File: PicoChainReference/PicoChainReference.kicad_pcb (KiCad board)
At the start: 2 copper layers, 60 x 34 mm, 16 parts, among them J1 RJ45, J2 RJ45, J3 +12V, J4 +5V(M), J5 SCL, J6 +5V, U2 PCA9615DP, U3 LM78M05, U4 LM78M05, U5 LM1085-12

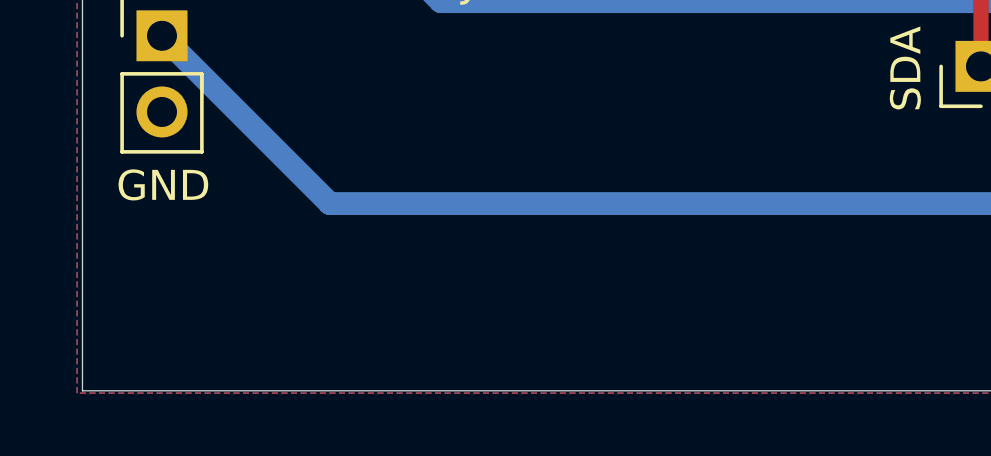
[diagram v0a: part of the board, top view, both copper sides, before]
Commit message: Finished off more reference designs and added readme
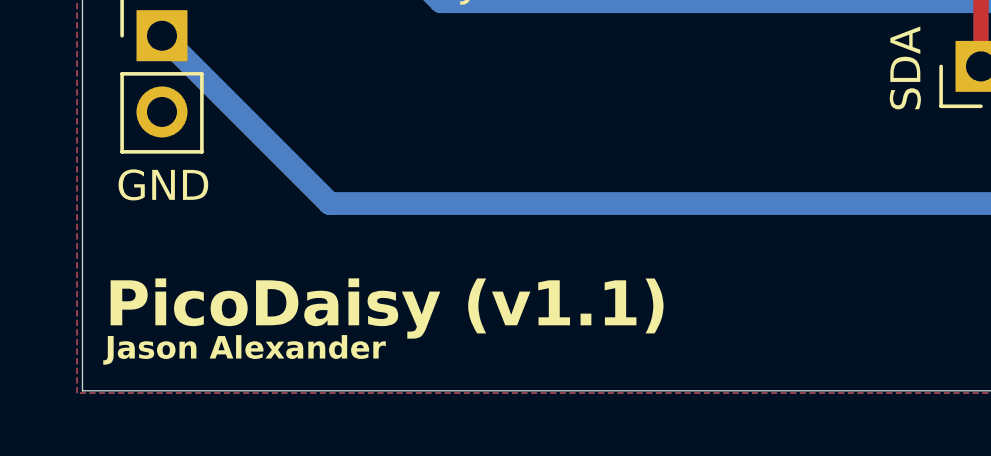
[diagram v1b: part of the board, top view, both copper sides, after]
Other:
- board text added: "Jason Alexander"
- board text added: "PicoDaisy (v1.1)"

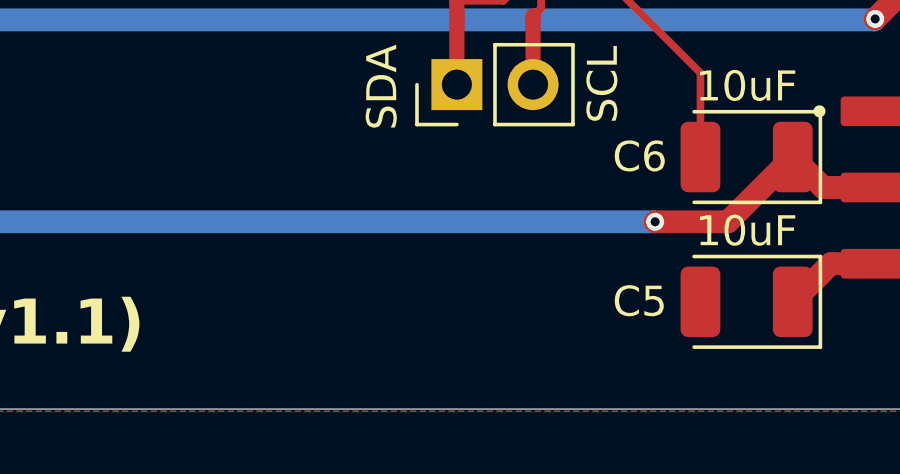
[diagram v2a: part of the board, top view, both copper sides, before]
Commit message: Added open source hardware logo to PCBs
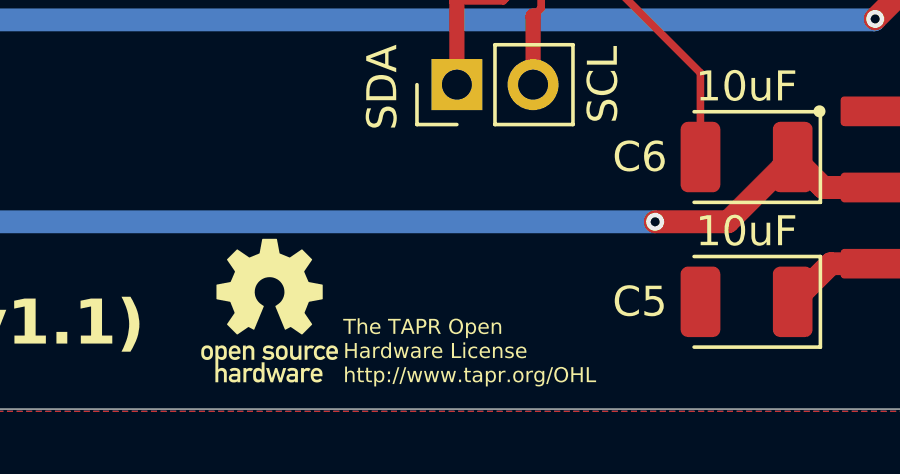
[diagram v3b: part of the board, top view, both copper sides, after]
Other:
- board text added: "The TAPR Open Hardware License http://www.tapr.org/OHL"

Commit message: Made pass through power rails larger.
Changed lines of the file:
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@@
 		(start 143.89475 86.99575)
 		(end 146.9545 83.936)
-		(width 0.762)
+		(width 1.016)
 		(layer "F.Cu")
 		(net 4)
@@
 		(start 143.8635 87.027)
 		(end 111.9455 87.027)
-		(width 0.762)
+		(width 1.016)
 		(layer "B.Cu")
 		(net 4)
@@
 		(start 111.9455 87.027)
 		(end 108.8545 83.936)
-		(width 0.762)
+		(width 1.016)
 		(layer "B.Cu")
 		(net 4)
@@
 		(start 116.4745 83.856)
 		(end 118.3755 85.757)
-		(width 0.762)
+		(width 1.016)
 		(layer "B.Cu")
 		(net 12)
@@
 		(start 118.3755 85.757)
 		(end 152.6735 85.757)
-		(width 0.762)
+		(width 1.016)
 		(layer "B.Cu")
 		(net 12)
@@
 		(start 152.6735 85.757)
 		(end 154.5745 83.856)
-		(width 0.762)
-		(layer "B.Cu")
-		(net 12)
+		(width 1.016)
+		(layer "B.Cu")
+		(net 12)

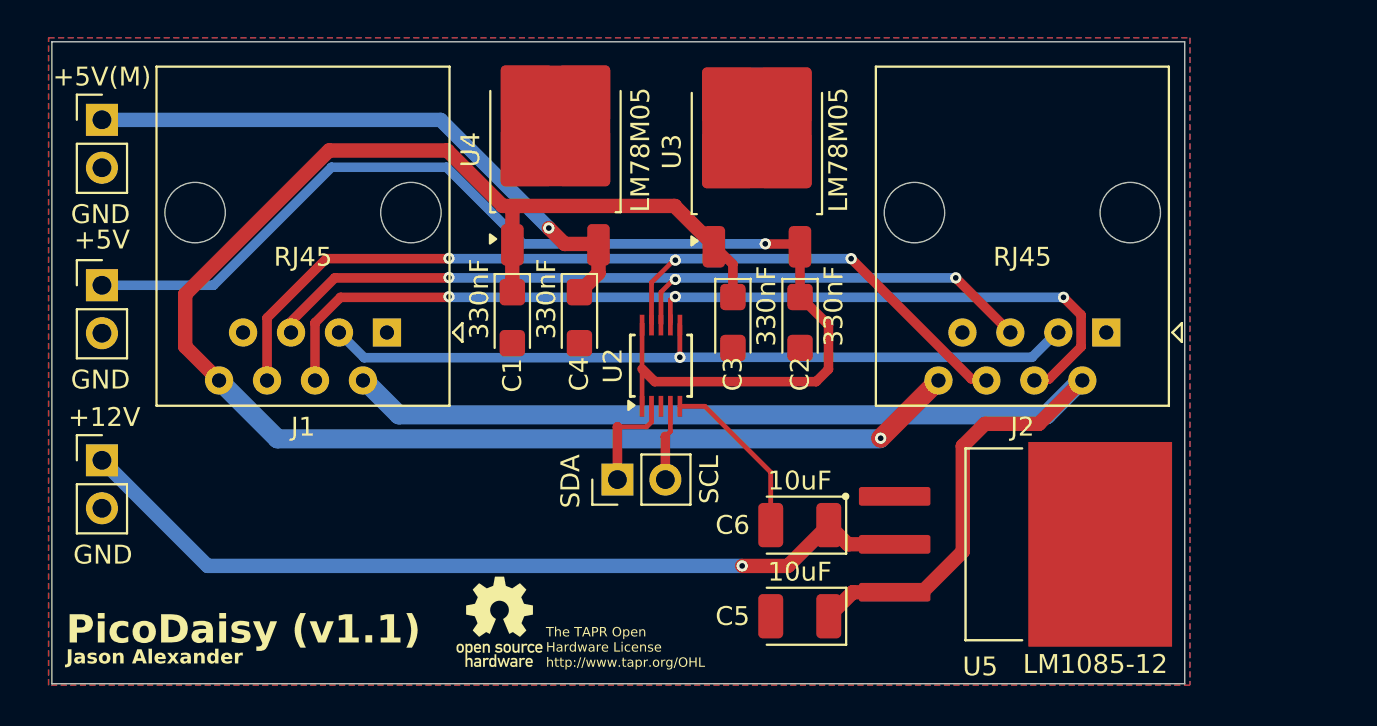
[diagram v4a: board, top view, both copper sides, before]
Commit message: Updated PicoChainZero base board.
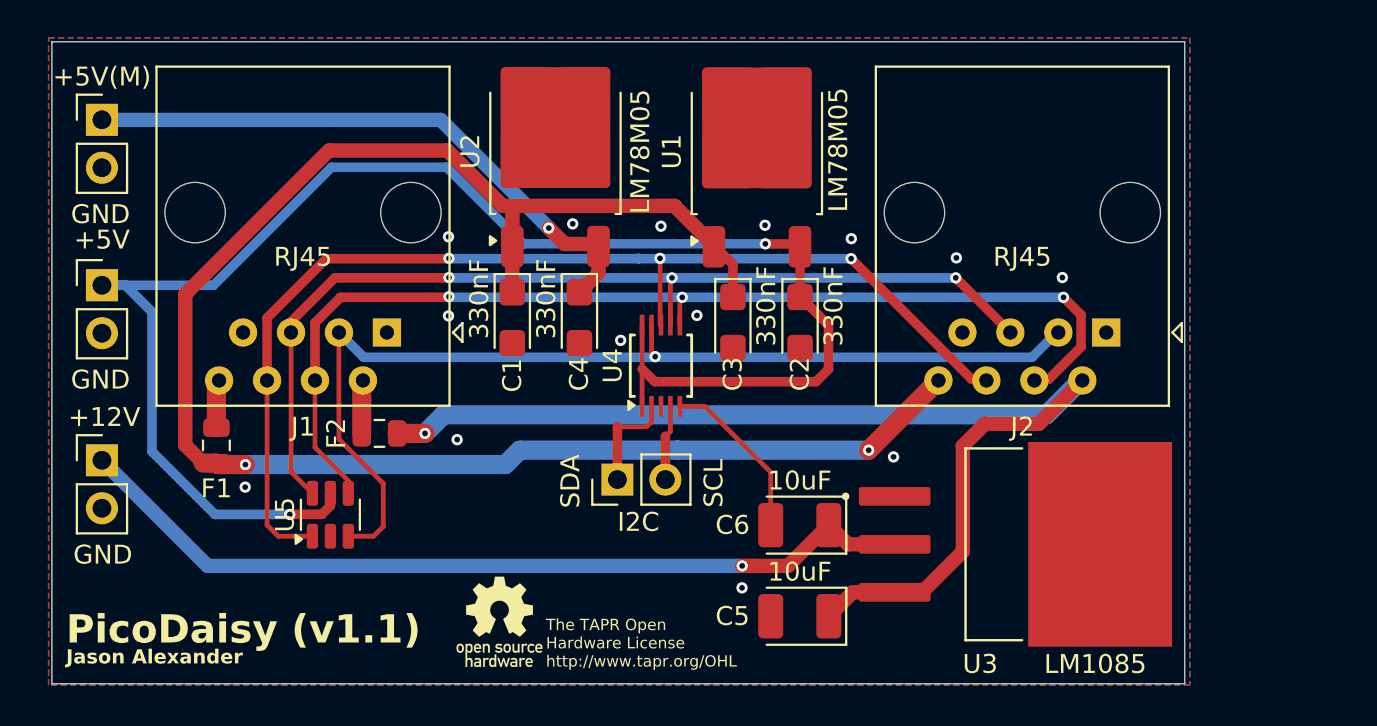
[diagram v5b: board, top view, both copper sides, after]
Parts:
- added F1: Fuse, Fuse:Fuse_0805_2012Metric, F.Cu at (108.7, 87.4)
- added F2: Fuse, Fuse:Fuse_0805_2012Metric, F.Cu at (117.3, 86.7)
- added U5: SRV05, Package_TO_SOT_SMD:SOT-23-6, F.Cu at (114.8, 91.0)
- J5: value SCL -> I2C
- U3: renamed from U5; value LM1085-12 -> LM1085
- moved U2 0.09 mm to (126.7, 71.8)
- renumbered U3 to U1, U4 to U2, U2 to U4
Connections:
- J1 pad 2: +24V -> Net-(F2-Pad1)
- J1 pad 3: Net-(U2-DSCLM) -> Net-(U4-DSDAM)
- J1 pad 4: Net-(U2-DSCLP) -> Net-(U4-DSCLM)
- J1 pad 5: Net-(U2-DSDAP) -> Net-(U4-DSCLP)
- J1 pad 6: Net-(U2-DSDAM) -> Net-(U4-DSDAP)
- J1 pad 8: +12V -> Net-(F1-Pad1)
- J2 pad 3: Net-(U2-DSCLM) -> Net-(U4-DSDAM)
- J2 pad 4: Net-(U2-DSCLP) -> Net-(U4-DSCLM)
- J2 pad 5: Net-(U2-DSDAP) -> Net-(U4-DSCLP)
- J2 pad 6: Net-(U2-DSDAM) -> Net-(U4-DSDAP)
- U4 pad 6: Net-(U2-DSCLM) -> Net-(U4-DSCLM)
- U4 pad 7: Net-(U2-DSCLP) -> Net-(U4-DSCLP)
- U4 pad 8: Net-(U2-DSDAP) -> Net-(U4-DSDAP)
- U4 pad 9: Net-(U2-DSDAM) -> Net-(U4-DSDAM)
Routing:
- net Net-(U4-DSDAP): track 0.00 -> 59.6 mm, vias 0 -> 3
- net Net-(U4-DSCLM): track 0.00 -> 57.2 mm, vias 0 -> 3
- net Net-(U4-DSDAM): track 0.00 -> 54.6 mm, vias 0 -> 1
- net Net-(U4-DSCLP): track 0.00 -> 52.3 mm, vias 0 -> 3
- net Net-(U2-DSCLP): track 50.6 -> 0.00 mm, vias 3 -> 0
- net Net-(U2-DSDAM): track 49.7 -> 0.00 mm, vias 3 -> 0
- net Net-(U2-DSDAP): track 43.5 -> 0.00 mm, vias 3 -> 0
- net Net-(U2-DSCLM): track 40.9 -> 0.00 mm, vias 1 -> 0
- net +5V: track 63.3 -> 85.7 mm, vias 1 -> 2
- net +12V: track 86.8 -> 91.0 mm, vias 1 -> 2
- net Net-(F2-Pad1): track 0.00 -> 2.83 mm
- net Net-(F1-Pad1): track 0.00 -> 2.56 mm
- net +24V: track 61.6 -> 59.4 mm, vias 0 -> 1
- net GND: vias 0 -> 14
- added copper zone on In1.Cu, net GND
- added copper zone on In2.Cu, net GND
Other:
- copper layers 2 -> 4
- board text added: "SCL"

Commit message: Updated to 1.2
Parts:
- U4: value PCA9615DP -> PCA9615
- moved J3 30.4 mm to (132.5, 93.7), turned to -90 degrees
- moved J4 27.5 mm to (120.4, 91.2)
- moved J6 25.2 mm to (124.7, 91.2)
- moved J2 1.95 mm to (157.8, 81.4)
- moved U5 1.26 mm to (113.5, 90.9)
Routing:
- net +5V: track 85.7 -> 52.4 mm, vias 2 -> 1
- net /+12V(R): track 45.6 -> 13.4 mm, vias 1 -> 0
- net /+5V(M): track 31.9 -> 18.0 mm, vias 1 -> 0
- net +24V: track 59.4 -> 63.3 mm
- net Net-(U4-DSDAM): track 54.6 -> 56.8 mm
- net +12V: track 91.0 -> 92.9 mm
- net Net-(U4-DSCLM): track 57.2 -> 55.3 mm
- net Net-(U4-DSCLP): track 52.3 -> 53.7 mm
- net GND: vias 14 -> 12
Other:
- board size 60 x 34 mm -> 68 x 34 mm
- board text added: "PicoDaisy (v1.2)"
- board text removed: "PicoDaisy (v1.1)"

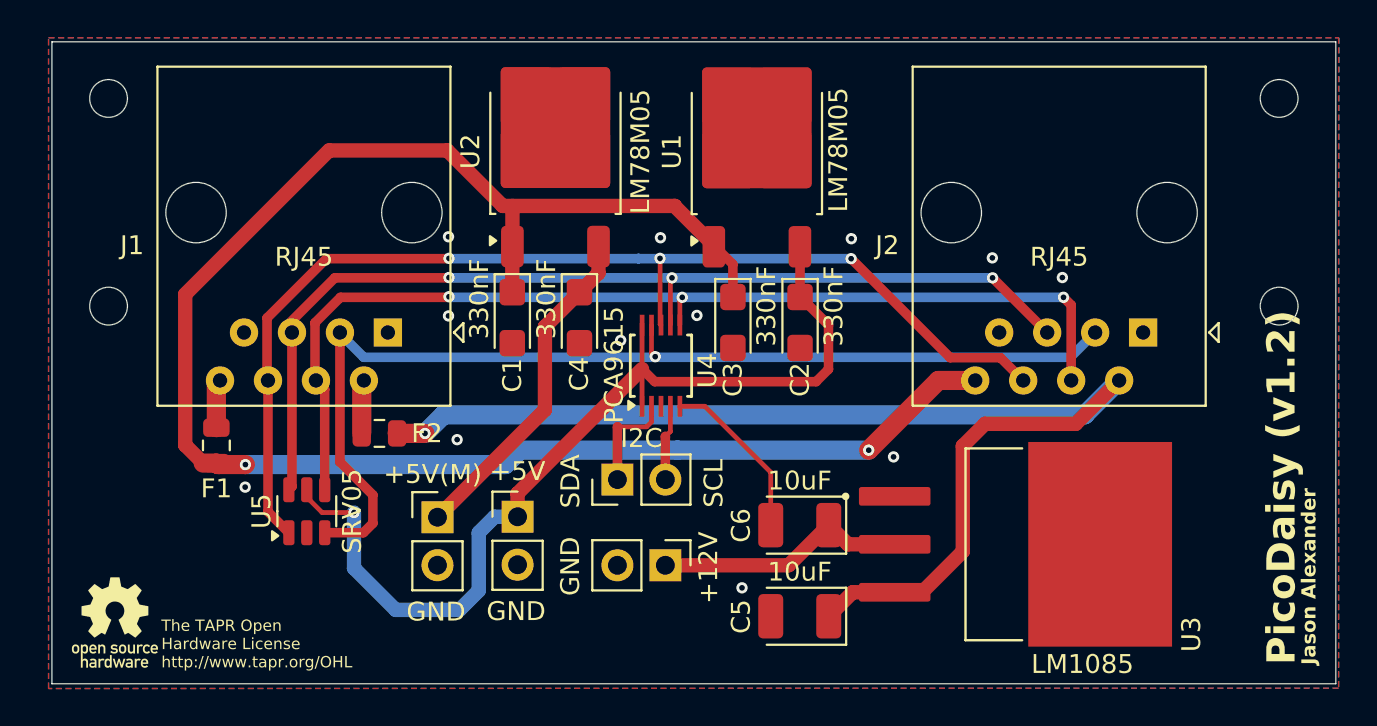
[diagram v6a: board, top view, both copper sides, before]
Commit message: Added more fuses to reference implementation
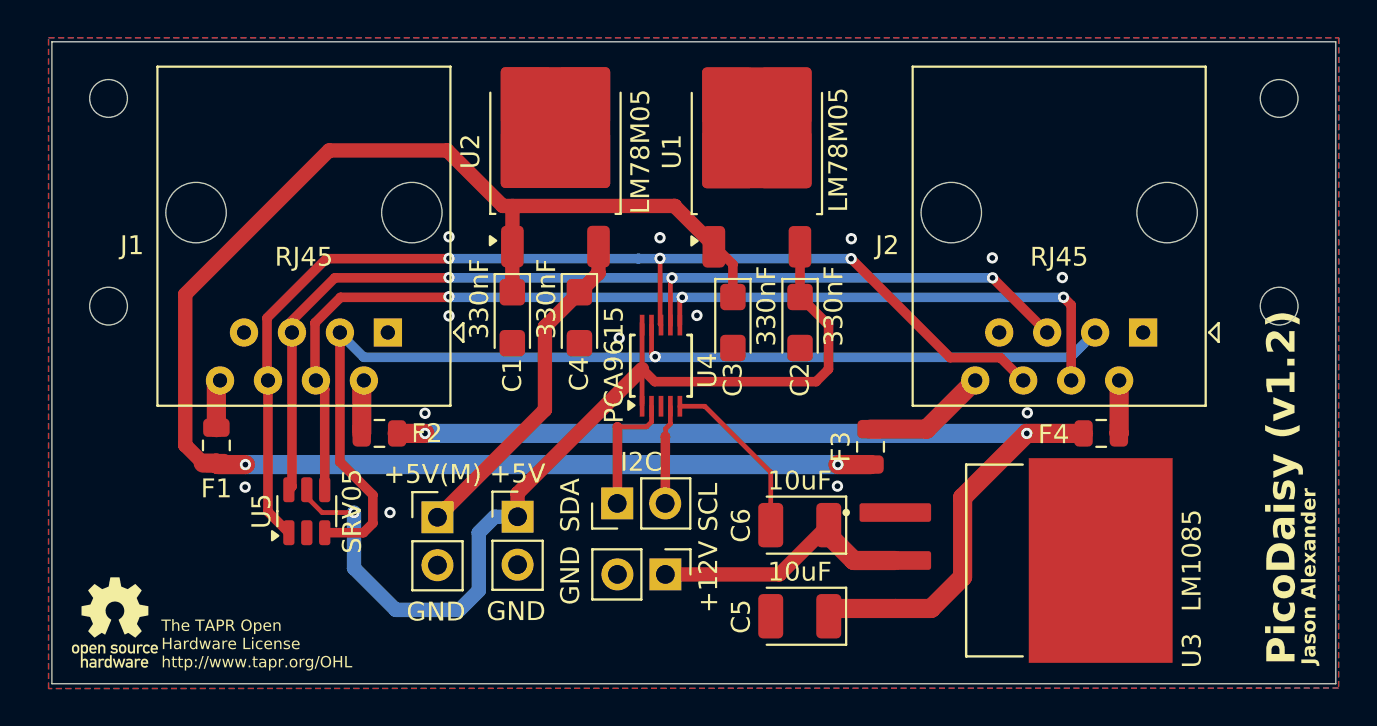
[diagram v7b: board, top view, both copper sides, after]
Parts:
- added F3: Fuse, Fuse:Fuse_0805_2012Metric, F.Cu at (143.4, 87.5)
- added F4: Fuse, Fuse:Fuse_0805_2012Metric, F.Cu at (155.6, 86.7)
- moved J5 1.26 mm to (129.9, 90.4)
- moved U3 0.86 mm to (151.1, 93.5)
- moved J3 0.48 mm to (132.5, 94.2)
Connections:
- J2 pad 2: +24V -> Net-(F4-Pad1)
- J2 pad 8: +12V -> Net-(F3-Pad1)
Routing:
- net +24V: track 63.3 -> 53.3 mm, vias 1 -> 2
- net +12V: track 92.9 -> 85.5 mm
- net Net-(F3-Pad1): track 0.00 -> 6.62 mm
- net Net-(F4-Pad1): track 0.00 -> 2.81 mm
- net Net-(J5-Pin_1): track 5.53 -> 6.80 mm
- net Net-(J5-Pin_2): track 3.99 -> 5.24 mm
- net /+12V(R): track 13.4 -> 14.4 mm
- net GND: vias 12 -> 13

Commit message: Updated example reference gerber files to remove extra inner PCB layers
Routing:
- net +24V: track 53.3 -> 52.4 mm
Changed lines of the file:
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@@
 			(psa4output no)
 			(plot_black_and_white yes)
-			(plotinvisibletext no)
 			(sketchpadsonfab no)
 			(plotpadnumbers no)
@@
 	)
 	(via
-		(at 119.761 85.6742)
+		(at 122.3518 85.3948)
 		(size 0.6)
 		(drill 0.3)
@@
 	)
 	(via
-		(at 110.236 89.5858)
+		(at 110.236 90.0684)
 		(size 0.6)
 		(drill 0.3)
@@
 	)
 	(via
-		(at 151.6634 85.6488)
+		(at 147.5232 87.9348)
 		(size 0.6)
 		(drill 0.3)
@@
 	)
 	(via
-		(at 117.9068 90.932)
+		(at 118.1354 90.932)
 		(size 0.6)
 		(drill 0.3)
@@
 	)
 	(via
-		(at 130.048 81.6864)
+		(at 129.7686 81.4324)
 		(size 0.6)
 		(drill 0.3)
@@
 	)
 	(via
-		(at 134.1628 80.4926)
+		(at 134.4676 80.518)
 		(size 0.6)
 		(drill 0.3)
@@
 	(segment
 		(start 154.6375 86.741)
-		(end 151.6326 86.741)
+		(end 149.5044 86.741)
 		(width 1.016)
 		(layer "F.Cu")
@@
 	)
 	(segment
-		(start 118.2855 86.741)
-		(end 119.761 86.741)
+		(start 146.564599 96.012)
+		(end 144.6696 96.012)
 		(width 1.016)
 		(layer "F.Cu")
@@
 	)
 	(segment
-		(start 151.6326 86.741)
-		(end 148.2344 90.1392)
+		(start 148.8186 93.757999)
+		(end 146.564599 96.012)
 		(width 1.016)
 		(layer "F.Cu")
@@
 	)
 	(segment
-		(start 146.564599 96.012)
-		(end 144.6696 96.012)
+		(start 149.5044 86.741)
+		(end 148.8186 87.4268)
 		(width 1.016)
 		(layer "F.Cu")
@@
 	)
 	(segment
-		(start 148.2344 94.342199)
-		(end 146.564599 96.012)
+		(start 148.8186 87.4268)
+		(end 148.8186 93.757999)
 		(width 1.016)
 		(layer "F.Cu")
@@
 	)
 	(segment
-		(start 148.2344 90.1392)
-		(end 148.2344 94.342199)
+		(start 141.5585 96.012)
+		(end 141.1455 96.425)
 		(width 1.016)
 		(layer "F.Cu")
@@
 	)
 	(segment
-		(start 141.5585 96.012)
-		(end 141.1455 96.425)
+		(start 144.6696 96.012)
+		(end 141.5585 96.012)
 		(width 1.016)
 		(layer "F.Cu")
@@
 	)
 	(segment
-		(start 144.6696 96.012)
-		(end 141.5585 96.012)
+		(start 118.2855 86.741)
+		(end 122.3518 86.741)
 		(width 1.016)
 		(layer "F.Cu")
@@
 	)
 	(via
-		(at 119.761 86.741)
+		(at 122.3518 86.741)
 		(size 0.6)
 		(drill 0.3)
@@
 	)
 	(via
-		(at 151.6326 86.741)
+		(at 149.5044 86.741)
 		(size 0.6)
 		(drill 0.3)
@@
 	)
 	(segment
-		(start 119.761 86.741)
-		(end 151.6326 86.741)
+		(start 122.3518 86.741)
+		(end 149.5044 86.741)
 		(width 1.016)
 		(layer "B.Cu")
